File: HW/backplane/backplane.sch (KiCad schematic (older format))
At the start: 5 parts

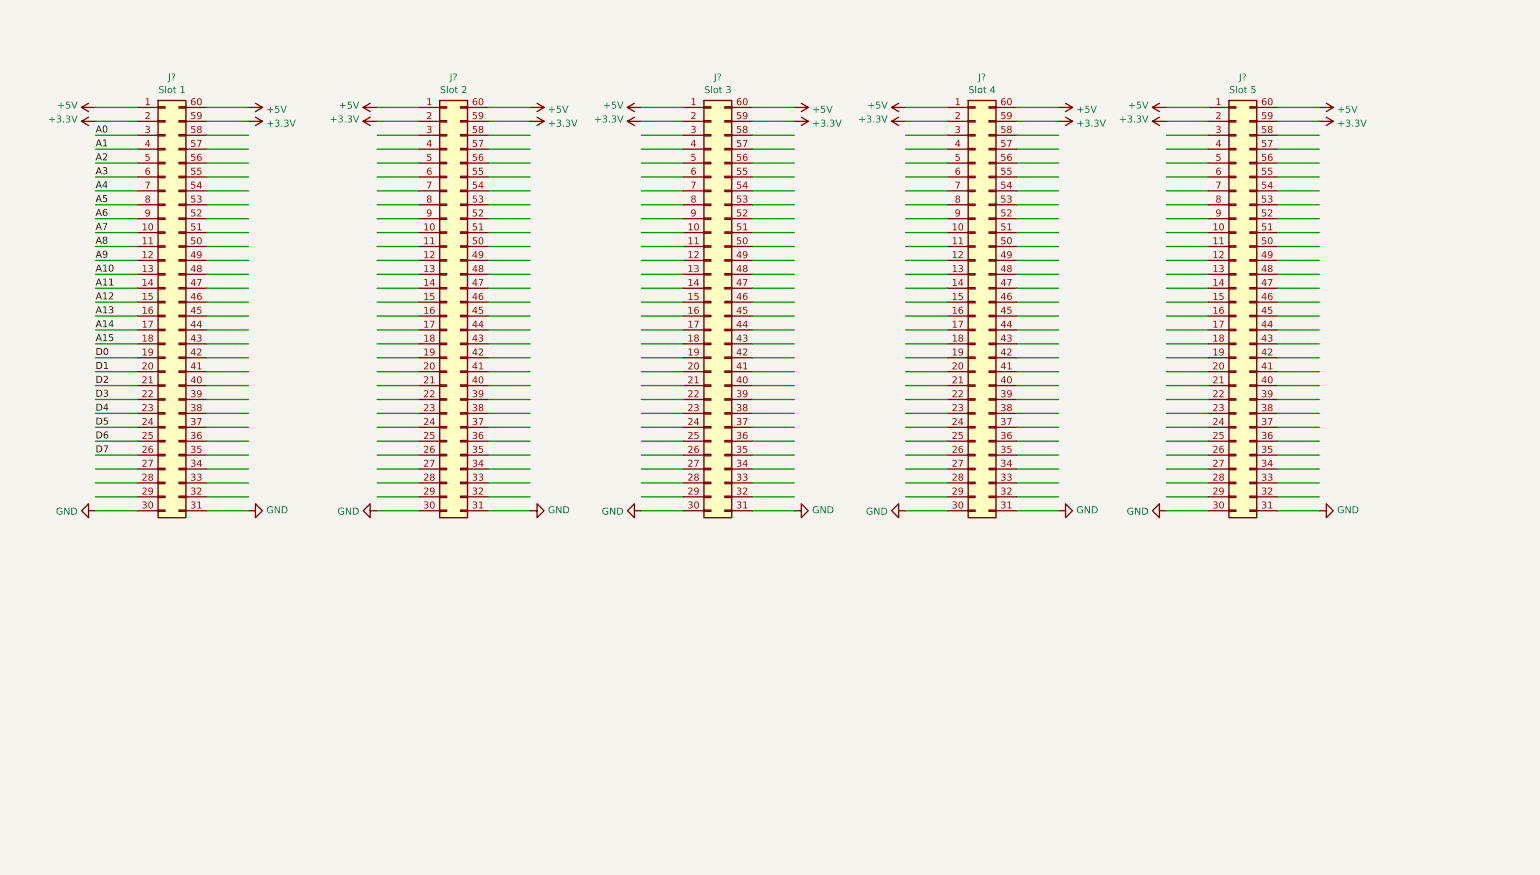
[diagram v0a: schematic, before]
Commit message: Restructure of directory tree.
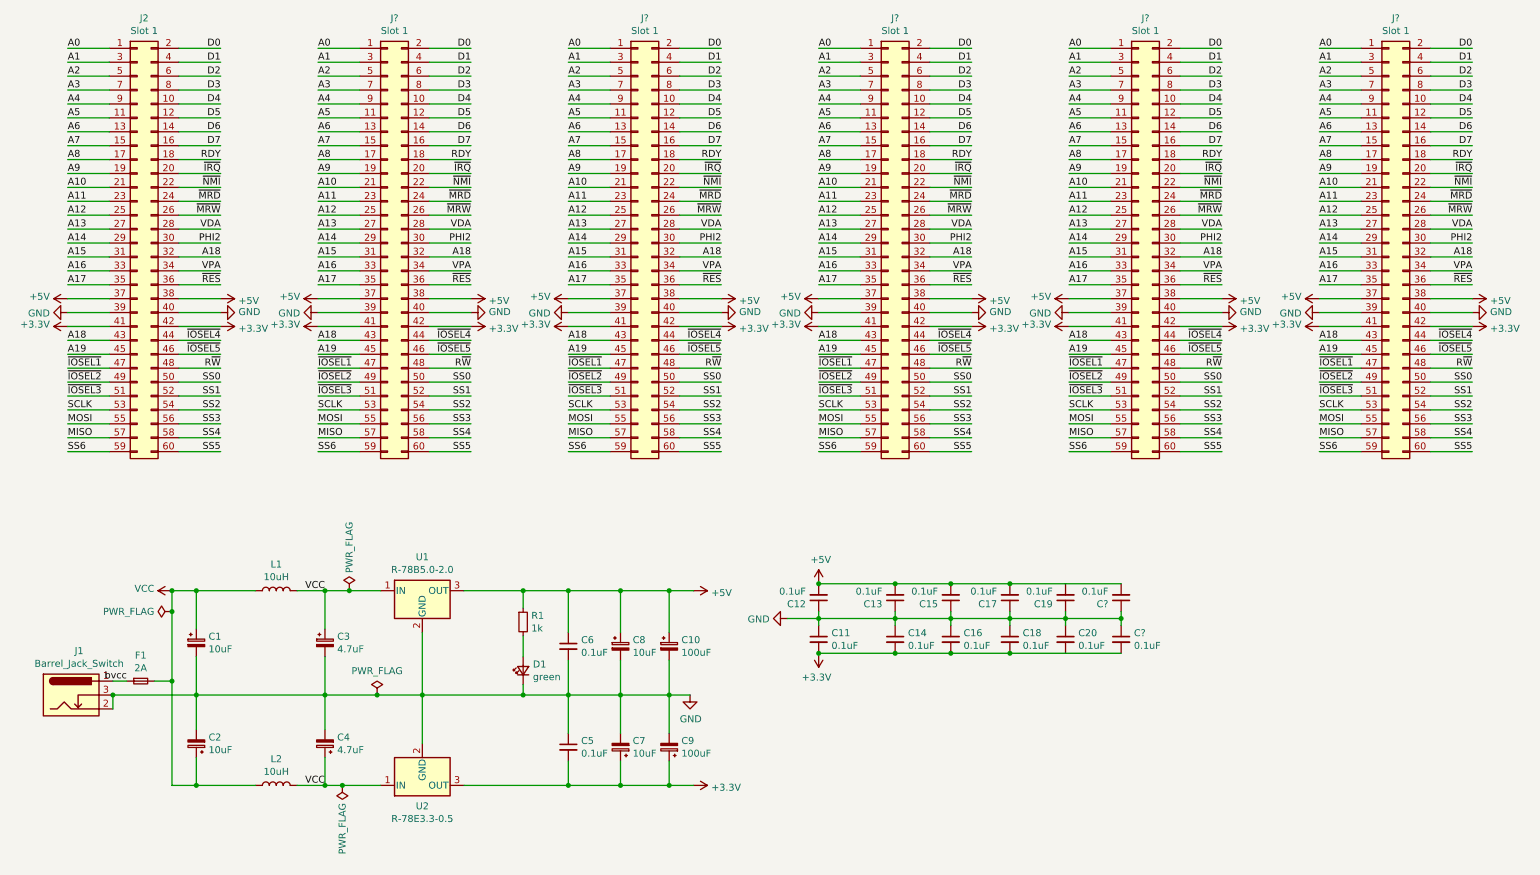
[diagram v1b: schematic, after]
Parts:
- removed J?: Slot 1, symbol Connector_Generic:Conn_02x30_Counter_Clockwise
- removed J?: Slot 2, symbol Connector_Generic:Conn_02x30_Counter_Clockwise
- removed J?: Slot 3, symbol Connector_Generic:Conn_02x30_Counter_Clockwise
- removed J?: Slot 4, symbol Connector_Generic:Conn_02x30_Counter_Clockwise
- removed J?: Slot 5, symbol Connector_Generic:Conn_02x30_Counter_Clockwise
- added C1, C2, C7, C8: 10uF, Capacitor_THT:CP_Radial_D5.0mm_P2.00mm, symbol Device:CP_Small
- added C10, C9: 100uF, Capacitor_THT:CP_Radial_D5.0mm_P2.00mm, symbol Device:CP_Small
- added C11, C12, C13, C14, C15, C16, C17, C18, C19, C20, C5, C6, C? (x2): 0.1uF, Capacitor_THT:C_Radial_D4.0mm_H5.0mm_P1.50mm, symbol Device:C_Small
- added C3, C4: 4.7uF, Capacitor_THT:CP_Radial_D5.0mm_P2.00mm, symbol Device:CP_Small
- added D1: green, LED_THT:LED_D3.0mm, symbol Device:LED_Small
- added F1: 2A, grotto:FUSE_0154004.DR, symbol Device:Fuse_Small
- added J1: Barrel_Jack_Switch, Connector_BarrelJack:BarrelJack_Horizontal, symbol Connector:Barrel_Jack_Switch
- added J2, J? (x5): Slot 1, Connector_PinSocket_2.54mm:PinSocket_2x30_P2.54mm_Vertical, symbol Connector_Generic:Conn_02x30_Odd_Even
- added L1, L2: 10uH, Inductor_THT:L_Radial_D7.0mm_P3.00mm, symbol Device:L
- added R1: 1k, Resistor_THT:R_Axial_DIN0411_L9.9mm_D3.6mm_P7.62mm_Vertical, symbol Device:R_Small
- added U1: R-78B5.0-2.0, Converter_DCDC:Converter_DCDC_RECOM_R-78B-2.0_THT, symbol Regulator_Switching:R-78B5.0-2.0
- added U2: R-78E3.3-0.5, Converter_DCDC:Converter_DCDC_RECOM_R-78E-0.5_THT, symbol Regulator_Switching:R-78E3.3-0.5
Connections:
- net labels added: A16, A17, A18, A19, MISO, MOSI, PHI2, RDY, R~W, SCLK, SS0, SS1, SS2, SS3, SS4, SS5, SS6, VCC, VDA, VPA, bvcc, ~IOSEL1, ~IOSEL2, ~IOSEL3, ~IOSEL4, ~IOSEL5, ~IRQ, ~MRD, ~MRW, ~NMI, ~RES
- wire segments 300 -> 447
